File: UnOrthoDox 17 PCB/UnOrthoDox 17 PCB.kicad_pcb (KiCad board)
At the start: 2 copper layers, 76.2 x 96.7 mm, 69 parts, among them SW1 SW_MX_HotSwap, SW10 SW_MX_HotSwap, SW11 SW_MX_HotSwap, SW12 SW_MX_HotSwap, SW13 SW_MX_HotSwap, SW14 SW_MX_HotSwap, SW15 SW_MX_HotSwap, SW16 SW_MX_HotSwap, SW17 SW_MX_HotSwap, SW18 SW_MX_HotSwap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

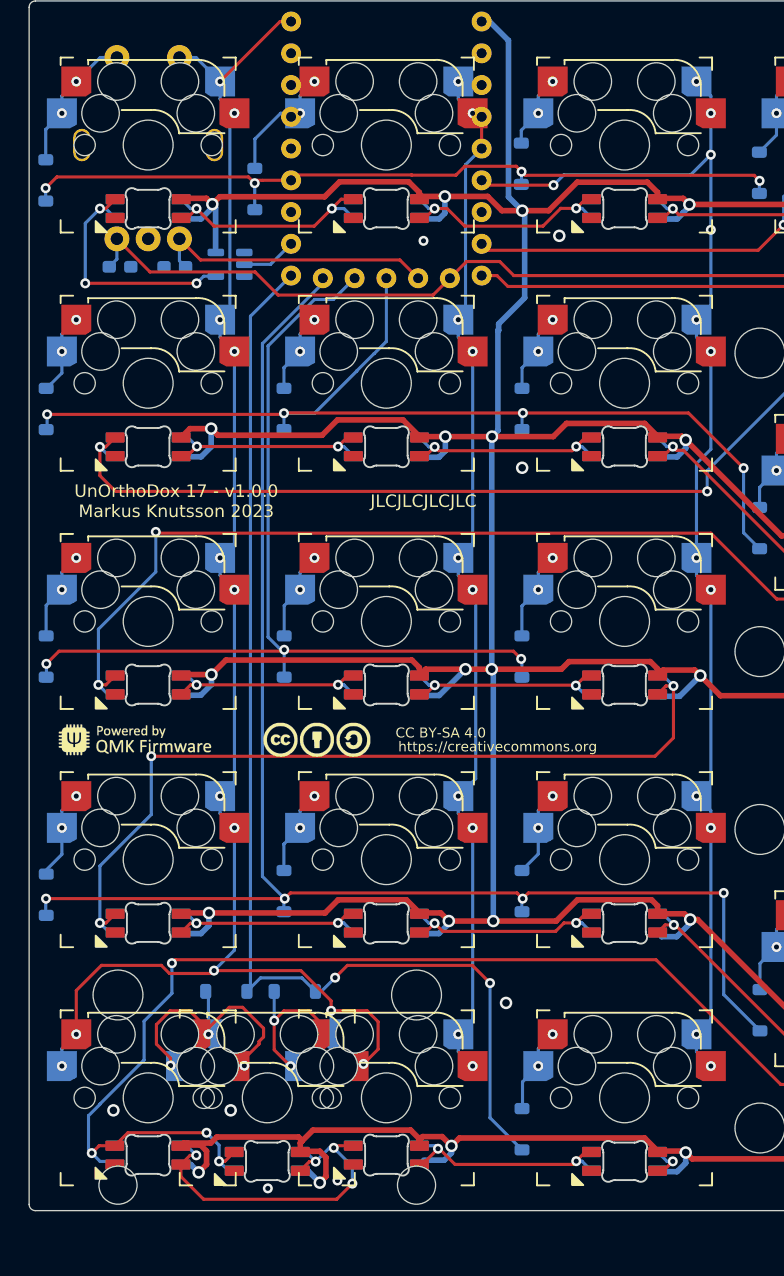
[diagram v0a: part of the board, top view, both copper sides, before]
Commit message: Final tweaks 17/20 PCB
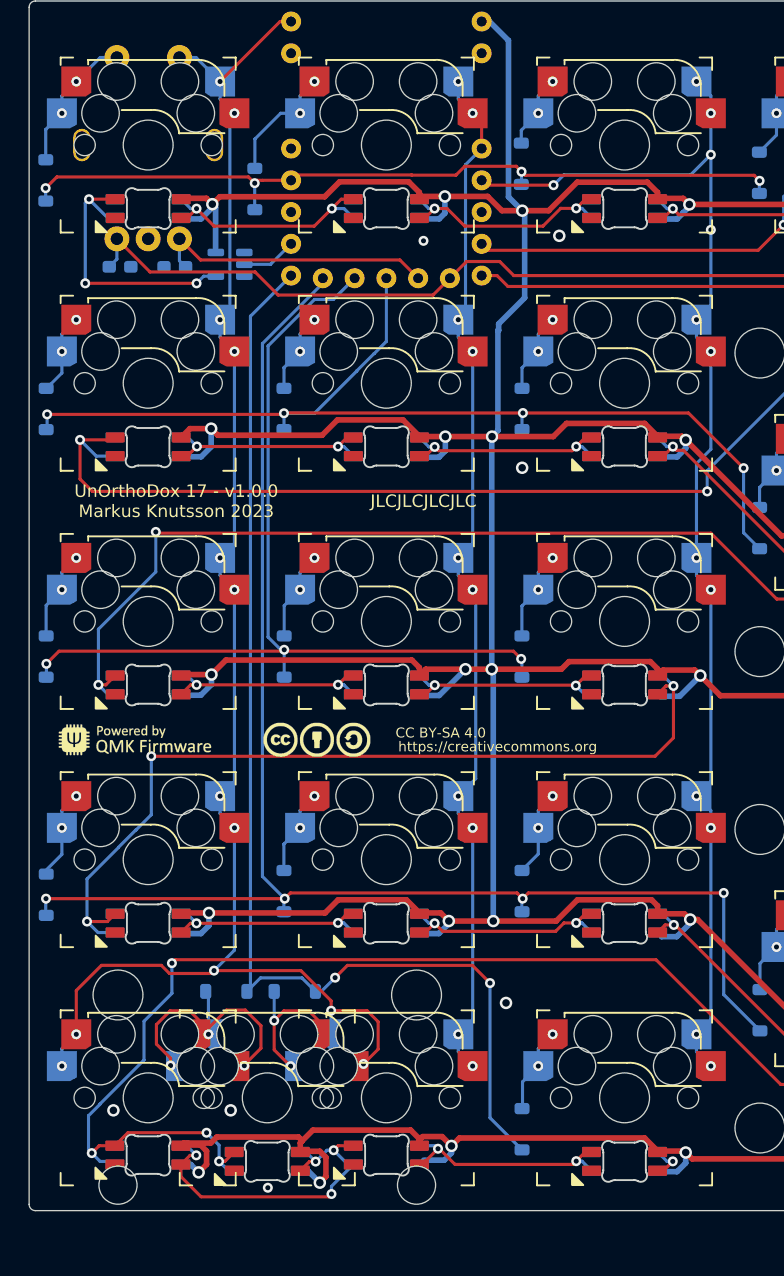
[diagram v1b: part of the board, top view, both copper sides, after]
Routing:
- net Net-(RGB4-DOUT): track 87.8 -> 93.3 mm
- net Net-(RGB11-DOUT): track 67.8 -> 70.2 mm
- net RGB_5: track 20.2 -> 22.3 mm
- net Net-(RGB16-DOUT): track 29.3 -> 28.6 mm
- net GND: vias 9 -> 8
